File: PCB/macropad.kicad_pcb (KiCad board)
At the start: 2 copper layers, 60 x 70.2 mm, 46 parts, among them J1 USB_C_Receptacle_USB2.0_16P, SW1 SW_Push, SW2 SW_Push, SW3 SW_Push, SW4 SW_Push, SW5 SW_Push, SW6 SW_Push, SW7 SW_Push, SW8 SW_Push, SW9 SW_Push, U1 ESP32-C6-MINI-1, U2 AZ1117CH2-3.3

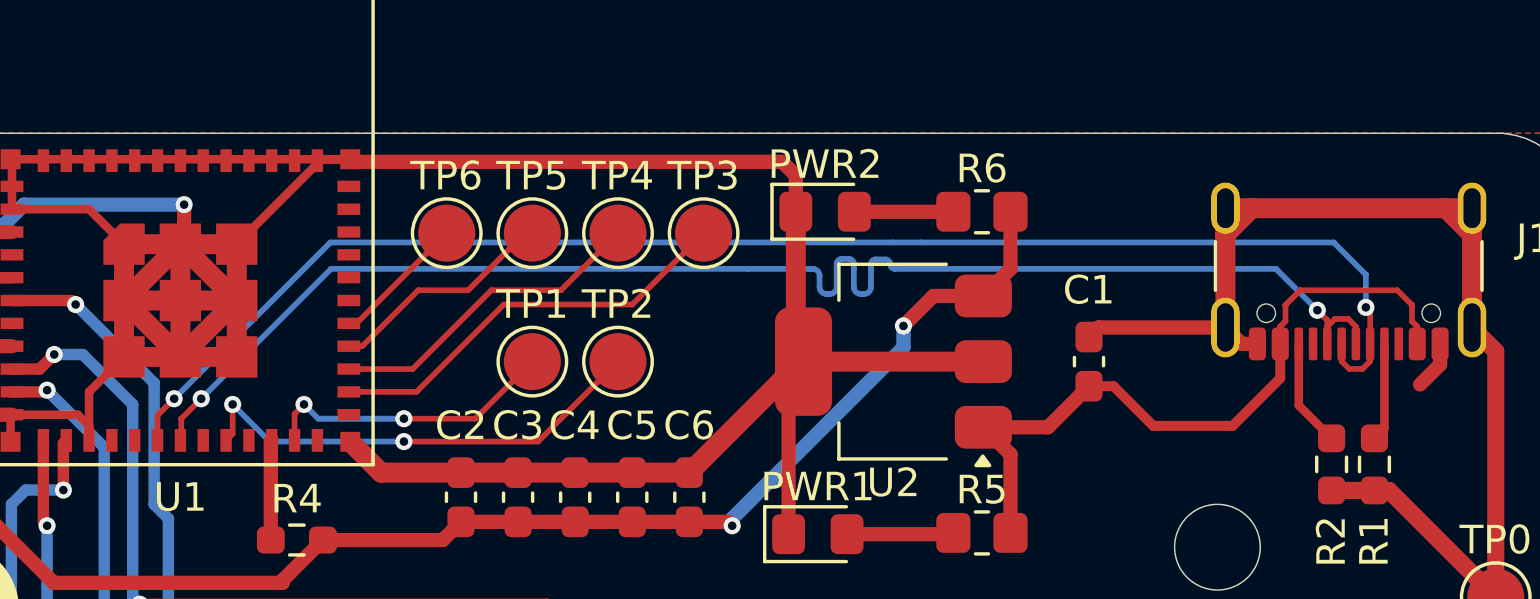
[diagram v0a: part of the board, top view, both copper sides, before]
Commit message: D+ D- traces
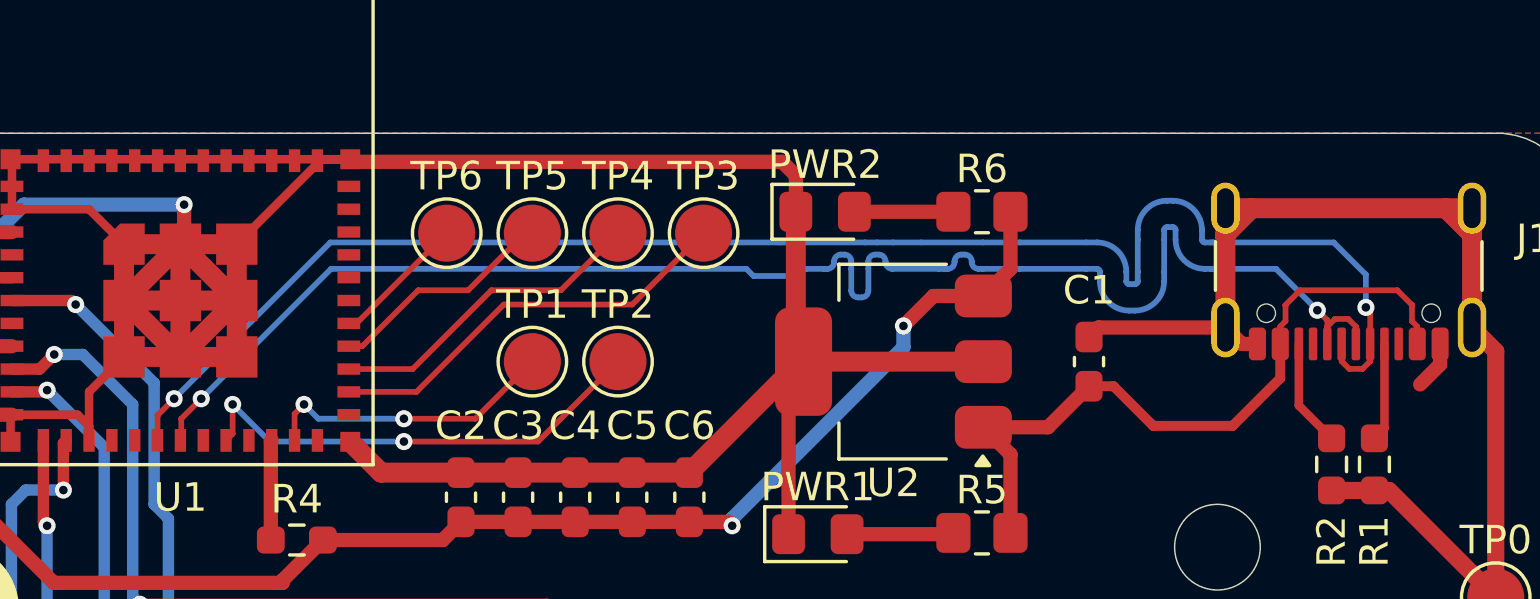
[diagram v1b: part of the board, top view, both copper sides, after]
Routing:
- net /D-: track 51.4 -> 55.6 mm
- net /D+: track 51.0 -> 55.2 mm
